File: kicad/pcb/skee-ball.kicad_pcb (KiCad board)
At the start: 2 copper layers, 107.6 x 91.5 mm, 62 parts, among them J13 HEADER, J18 DC_DRIVER, J19 JOYSTICK, J2 EXTERNAL_BUTTON, J20 SERVO, J21 US0, J22 US1, J26 US2, J27 US3, J3 Conn_02x06_Counter_Clockwise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

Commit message: minor changes to schematic
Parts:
- J3: value Conn_02x06_Counter_Clockwise -> OLED_CONN1
- J5: value Conn_01x05 -> OLED_CONN2
- moved J4 3.05 mm to (81.0, 45.6)
- moved H4 2.34 mm to (73.0, 113.8)
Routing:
- net +5V: track 237.3 -> 226.7 mm
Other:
- board size 107.6 x 91.5 mm -> 101.6 x 101.6 mm
- board text added: "BTN+"
- board text added: "BTN-"
- board text removed: "BUTTON+"
- board text removed: "BUTTON-"
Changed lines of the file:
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@@
 		(allow_soldermask_bridges_in_footprints no)
 		(tenting front back)
+		(grid_origin 62.864959 26.817682)
 		(pcbplotparams
 			(layerselection 0x00000000_00000000_55555555_5755f5ff)
@@
 	(footprint "Connector_BarrelJack:BarrelJack_CUI_PJ-063AH_Horizontal"
 		(layer "F.Cu")
-		(at 77.9154 45.6184 -90)
+		(at 80.963359 45.562882 -90)
 		(descr "Barrel Jack, 2.0mm ID, 5.5mm OD, 24V, 8A, no switch, https://www.cui.com/product/resource/pj-063ah.pdf")
 		(tags "barrel jack cui dc power")
@@
 			)
 		)
-		(property "Datasheet" "https://www.st.com/resource/en/datasheet/stm32f091rc.pdf"
+		(property "Datasheet" "https://engineering.purdue.edu/477grp1/Files/refs/stm32f091cc.pdf"
 			(at 0 0 0)
 			(layer "F.Fab")
@@
 			)
 		)
-		(property "Value" "Conn_01x05"
+		(property "Value" "OLED_CONN2"
 			(at 0 12.49 0)
 			(layer "F.Fab")
@@
 			)
 		)
-		(property "Datasheet" "sfgsdfgsdfg"
+		(property "Datasheet" "https://engineering.purdue.edu/477grp1/Files/refs/d24v22f6.pdf"
 			(at 0 0 90)
 			(layer "F.Fab")
@@
 			)
 		)
-		(property "Description" ""
+		(property "Description" "24V - 6V Regulator"
 			(at 0 0 90)
 			(layer "F.Fab")
@@
 	(footprint "MountingHole:MountingHole_3.2mm_M3"
 		(layer "F.Cu")
-		(at 70.6882 113.8428)
+		(at 73.024959 113.8428)
 		(descr "Mounting Hole 3.2mm, no annular, M3")
 		(tags "mounting hole 3.2mm no annular m3")
@@
 			)
 		)
-		(property "Value" "Conn_02x06_Counter_Clockwise"
+		(property "Value" "OLED_CONN1"
 			(at 1.27 15.03 0)
 			(layer "F.Fab")
@@
 			)
 		)
-		(property "Datasheet" ""
+		(property "Datasheet" "https://engineering.purdue.edu/477grp1/Files/refs/d24v22f5.pdf"
 			(at 0 0 90)
 			(layer "F.Fab")
@@
 			)
 		)
-		(property "Description" ""
+		(property "Description" "24V - 5V Regulator"
 			(at 0 0 90)
 			(layer "F.Fab")
@@
 	(gr_poly
 		(pts
-			(xy 62.864959 26.817682) (xy 170.385891 26.845777) (xy 170.354024 118.334446) (xy 62.833092 118.306351)
+			(xy 68.548976 26.819168) (xy 170.133223 26.845712) (xy 170.097844 128.416913) (xy 68.513598 128.417642)
 		)
 		(stroke
@@
 		)
 	)
-	(gr_text "BUTTON+"
-		(at 163.449 96.4692 0)
+	(gr_text "BTN+"
+		(at 164.058559 96.4692 0)
 		(layer "F.SilkS")
 		(effects
@@
 		)
 	)
-	(gr_text "BUTTON-"
-		(at 163.449 93.5228 0)
+	(gr_text "BTN-"
+		(at 164.007759 93.467282 0)
 		(layer "F.SilkS")
 		(effects
@@
 	)
 	(segment
+		(start 75.532641 53.75)
+		(end 74.264959 55.017682)
+		(width 0.2)
+		(layer "B.Cu")
+		(net 39)
+	)
+	(segment
 		(start 115.7986 57.8104)
 		(end 115.7986 63.7032)
@@
 	)
 	(segment
+		(start 74.264959 99.6508)
+		(end 76.264959 101.6508)
+		(width 0.2)
+		(layer "B.Cu")
+		(net 39)
+	)
+	(segment
 		(start 160.9282 56.4388)
 		(end 160.9282 57.574)
@@
 	)
 	(segment
-		(start 67.25 59)
-		(end 67.25 97.75)
+		(start 90.5 53.75)
+		(end 75.532641 53.75)
 		(width 0.2)
 		(layer "B.Cu")
@@
 	)
 	(segment
-		(start 114.8969 64.6049)
-		(end 114.1984 65.3034)
+		(start 74.264959 55.017682)
+		(end 74.264959 99.6508)
 		(width 0.2)
 		(layer "B.Cu")
@@
 	)
 	(segment
-		(start 71.1508 101.6508)
-		(end 74.0992 101.6508)
+		(start 114.8969 64.6049)
+		(end 114.1984 65.3034)
 		(width 0.2)
 		(layer "B.Cu")
@@
 	)
 	(segment
-		(start 72.5 53.75)
-		(end 67.25 59)
-		(width 0.2)
-		(layer "B.Cu")
-		(net 39)
-	)
-	(segment
 		(start 91.4146 101.6508)
 		(end 91.7702 101.2952)
@@
 	)
 	(segment
-		(start 74.0992 101.6508)
+		(start 76.264959 101.6508)
 		(end 84.1502 101.6508)
 		(width 0.2)
@@
 	)
 	(segment
-		(start 67.25 97.75)
-		(end 71.1508 101.6508)
-		(width 0.2)
-		(layer "B.Cu")
-		(net 39)
-	)
-	(segment
 		(start 158.0348 87.9896)
 		(end 156.7434 87.9896)
@@
 	)
 	(segment
-		(start 90.5 53.75)
-		(end 72.5 53.75)
-		(width 0.2)
-		(layer "B.Cu")
-		(net 39)
-	)
-	(segment
 		(start 115.8494 65.532)
 		(end 115.8494 78.4098)
@@
 		(polygon
 			(pts
-				(xy 76.715241 50.720529) (xy 75.149373 50.7238) (xy 75.061369 40.051045) (xy 77.978 40.1066) (xy 82.0928 40.132)
-				(xy 82.042 45.4406) (xy 92.01749 45.523042) (xy 92.171242 48.290604) (xy 82.057516 48.382209) (xy 82.072161 61.899658)
-				(xy 82.1182 65.7098) (xy 86.7156 65.6336) (xy 86.7664 68.1736) (xy 82.07893 68.148129) (xy 76.696389 68.121745)
+				(xy 76.715241 50.720529) (xy 77.619079 50.718641) (xy 77.531505 40.098096) (xy 77.978 40.1066) (xy 83.208718 40.138889)
+				(xy 83.234133 45.378098) (xy 92.01749 45.523042) (xy 92.024159 48.255282) (xy 82.057516 48.382209)
+				(xy 82.072161 61.899658) (xy 82.1182 65.7098) (xy 86.7156 65.6336) (xy 86.7664 68.1736) (xy 82.07893 68.148129)
+				(xy 76.696389 68.121745)
 			)
 		)
@@
 		(polygon
 			(pts
-				(xy 63.8734 107.016685) (xy 111.5822 106.934) (xy 111.633 96.1898) (xy 142.773075 95.800245) (xy 142.874491 106.930552)
-				(xy 170 107) (xy 170 35) (xy 102.520353 34.864427) (xy 81.534451 35.013804) (xy 63.8734 35.139515)
+				(xy 69.7662 107.006472) (xy 111.5822 106.934) (xy 111.633 96.1898) (xy 142.773075 95.800245) (xy 142.874491 106.930552)
+				(xy 169.492 106.9987) (xy 169.492 34.998979) (xy 102.520353 34.864427) (xy 81.534451 35.013804)
+				(xy 69.7662 35.097571)
 			)
 		)

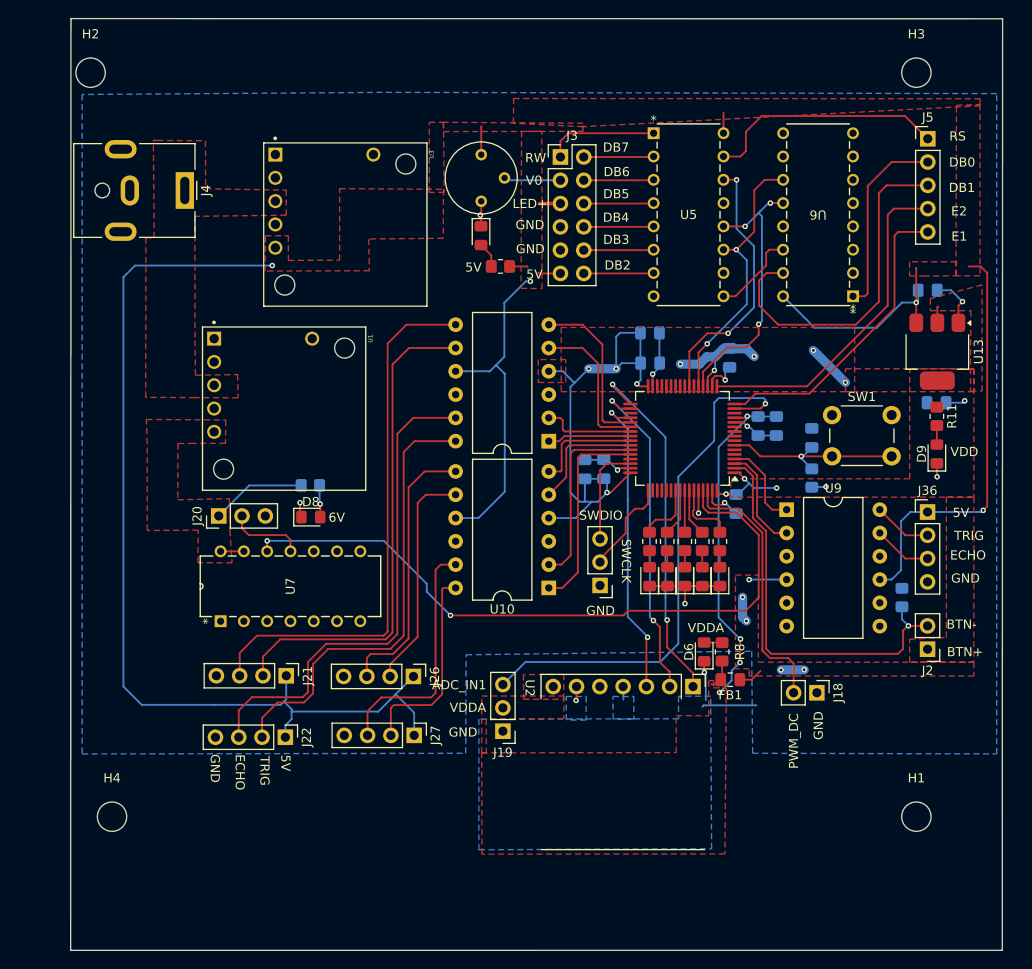
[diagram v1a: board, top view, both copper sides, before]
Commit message: reposition pcb mounting holes
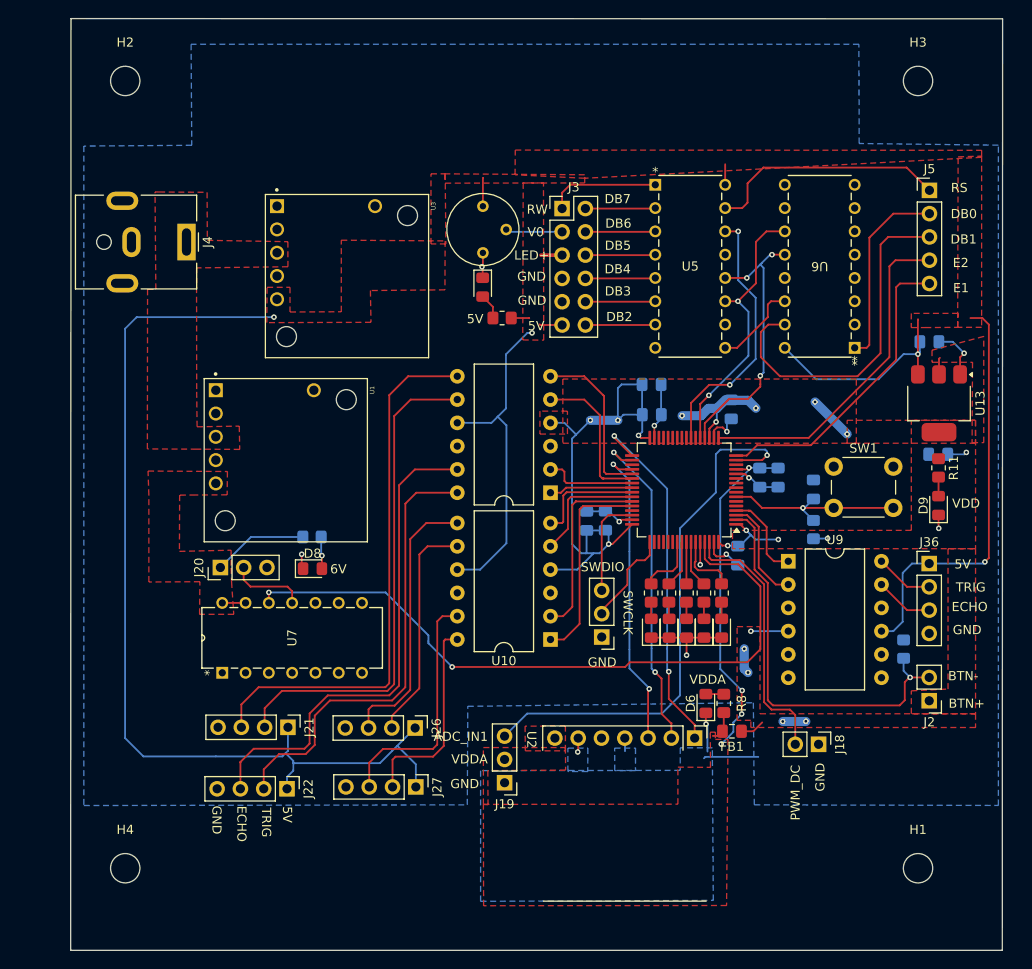
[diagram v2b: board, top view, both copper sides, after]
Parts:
- moved H4 5.80 mm to (74.5, 119.5)
- moved C7 5.63 mm to (163.1, 74.3)
- moved R1 5.63 mm to (149.5, 82.5)
- moved J5 5.63 mm to (162.2, 45.5)
- moved D7 5.63 mm to (113.4, 56.1)
- moved J3 5.63 mm to (122.1, 47.5)
- moved RV1 5.63 mm to (113.5, 47.3)
- moved U13 5.63 mm to (163.2, 68.8)
- moved C10 5.63 mm to (140.5, 69.4)
- moved C14 5.63 mm to (141.3, 85.4)
- moved C6 5.63 mm to (162.1, 62.1)
- moved D1 5.63 mm to (135.7, 93.3)
- moved D3 5.63 mm to (139.5, 93.3)
- moved D5 5.63 mm to (133.8, 93.3)
- moved D9 5.63 mm to (163.1, 79.9)
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
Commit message: update silkscreen
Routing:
- net VDD: track 102.2 -> 96.5 mm, vias 19 -> 21
- net GND: track 63.1 -> 64.8 mm, vias 13 -> 17
- net +5V: track 226.7 -> 227.6 mm
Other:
- board text added: "D24V22F5"
- board text added: "D24V22F6"
- board text added: "Revision #1"
- board text added: "U2"
